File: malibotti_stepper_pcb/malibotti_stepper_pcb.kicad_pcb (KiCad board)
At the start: 2 copper layers, 70 x 68 mm, 65 parts, among them J1 Stepper 1, J2 Stepper 1, J3 Servo, J4 Conn_01x04, J5 USB_C_Receptacle_USB2.0_16P, J6 Conn_01x04, SW1 RST, SW2 MicroSwitchLeft, SW3 MicroSwitchRight, SW8 BTN, U1 ESP32-C3-MINI-1, U2 XC6206PxxxMR, U3 STSPIN220, U4 STSPIN220

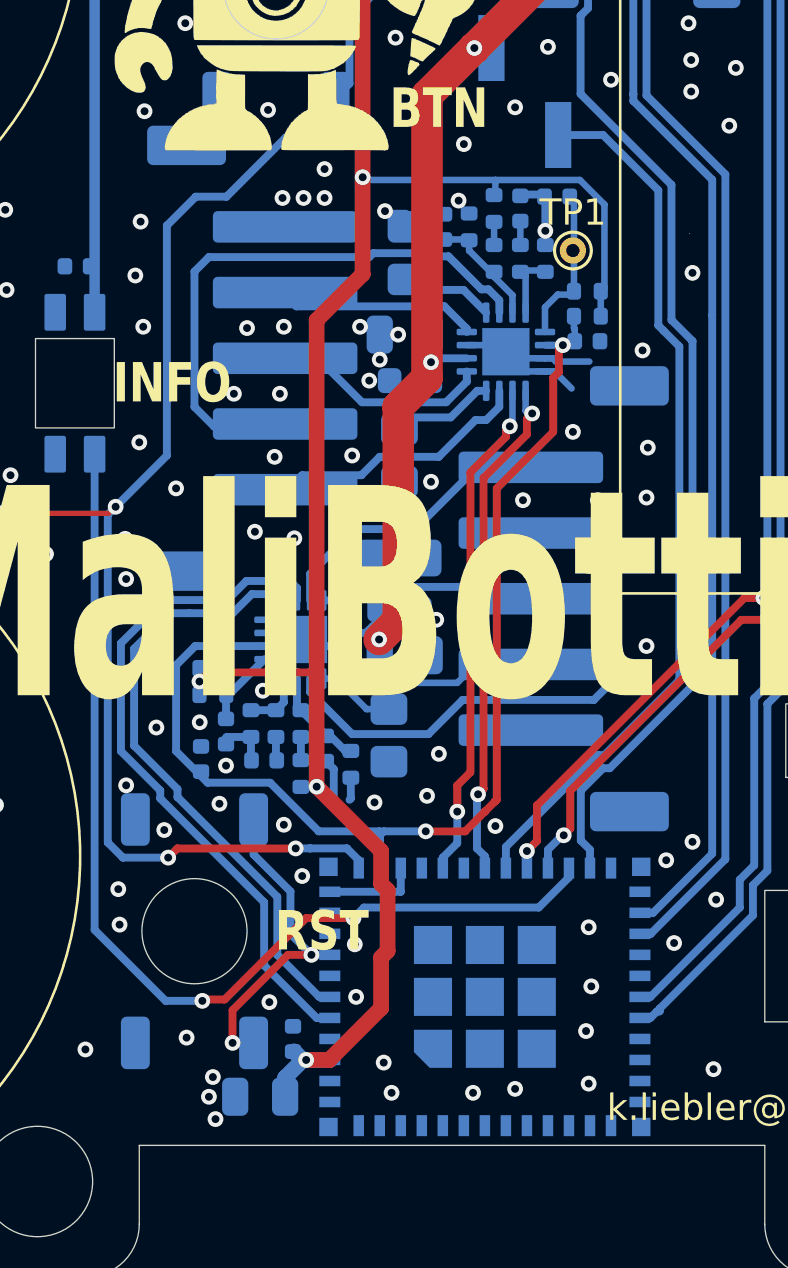
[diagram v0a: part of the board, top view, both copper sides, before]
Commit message: Malibotti unipolar as ordered @ JLCPCB
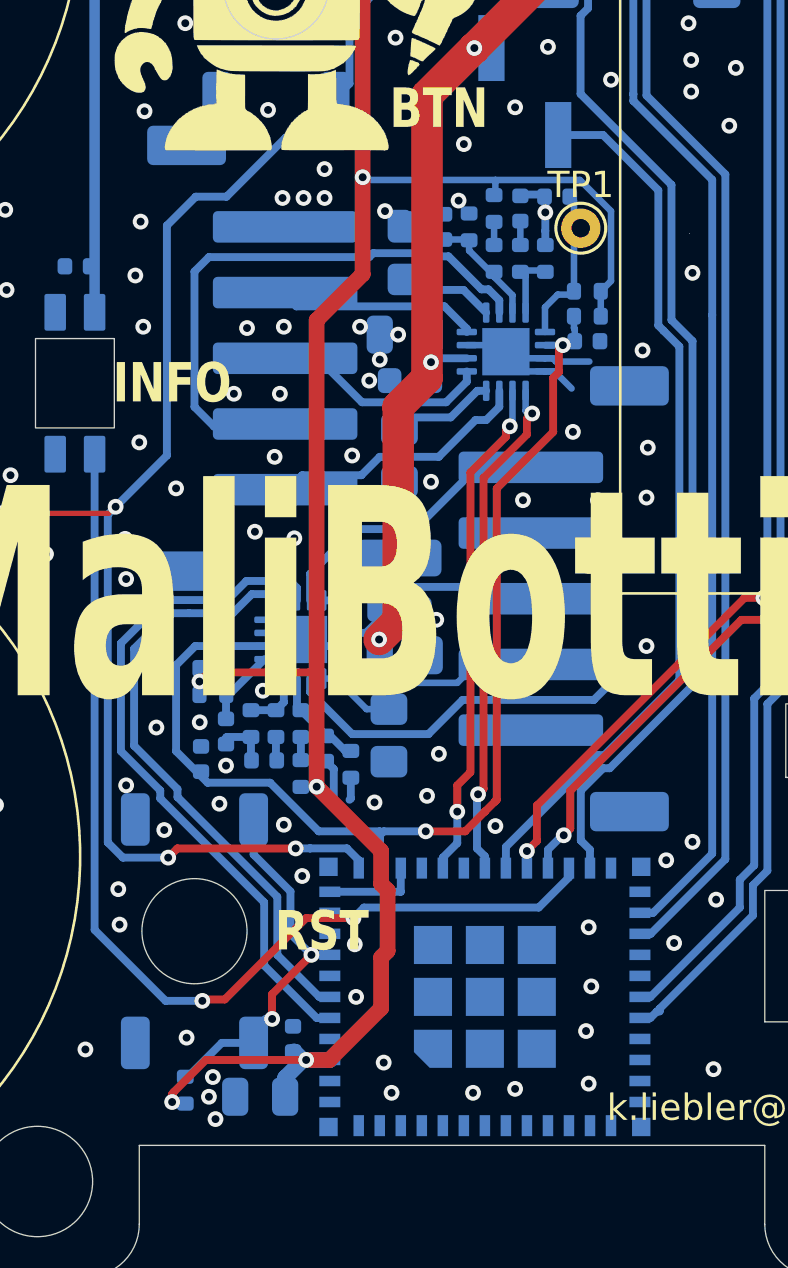
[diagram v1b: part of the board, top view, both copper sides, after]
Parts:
- added R26: 10k, Resistor_SMD:R_0402_1005Metric, B.Cu at (84.0, 126.9)
- J2: value Stepper 1 -> Stepper 2
- J4: value Conn_01x04 -> I2C
- TP1: footprint TestPoint:TestPoint_THTPad_D1.0mm_Drill0.5mm -> TestPoint:TestPoint_THTPad_D1.5mm_Drill0.7mm
- moved TP1 0.90 mm to (99.0, 94.1)
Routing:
- net +3V3: track 109.6 -> 116.3 mm, vias 4 -> 5
- net Net-(U1-EN/CHIP_PU): track 12.7 -> 14.3 mm
- net GND: vias 152 -> 151
